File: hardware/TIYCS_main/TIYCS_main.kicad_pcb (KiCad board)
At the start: 2 copper layers, 100 x 100 mm, 46 parts, among them J1 USB4105-GF-A, J2 12vPWM, J3 WS2812B, J4 UART, J5 ExtSensor, J6 Terminal, J7 Barrel_Jack_Switch, J8 pinHeaders, Q1 NCE4060K, Q2 NCE4060K, Q3 2N7002, Q4 NCE4060K, Q5 NCE4060K, SW1 RST, SW2 BOOT, U1 ESP32-WROOM-32U, U2 CH340N, U3 SPX3819M5-L-3-3

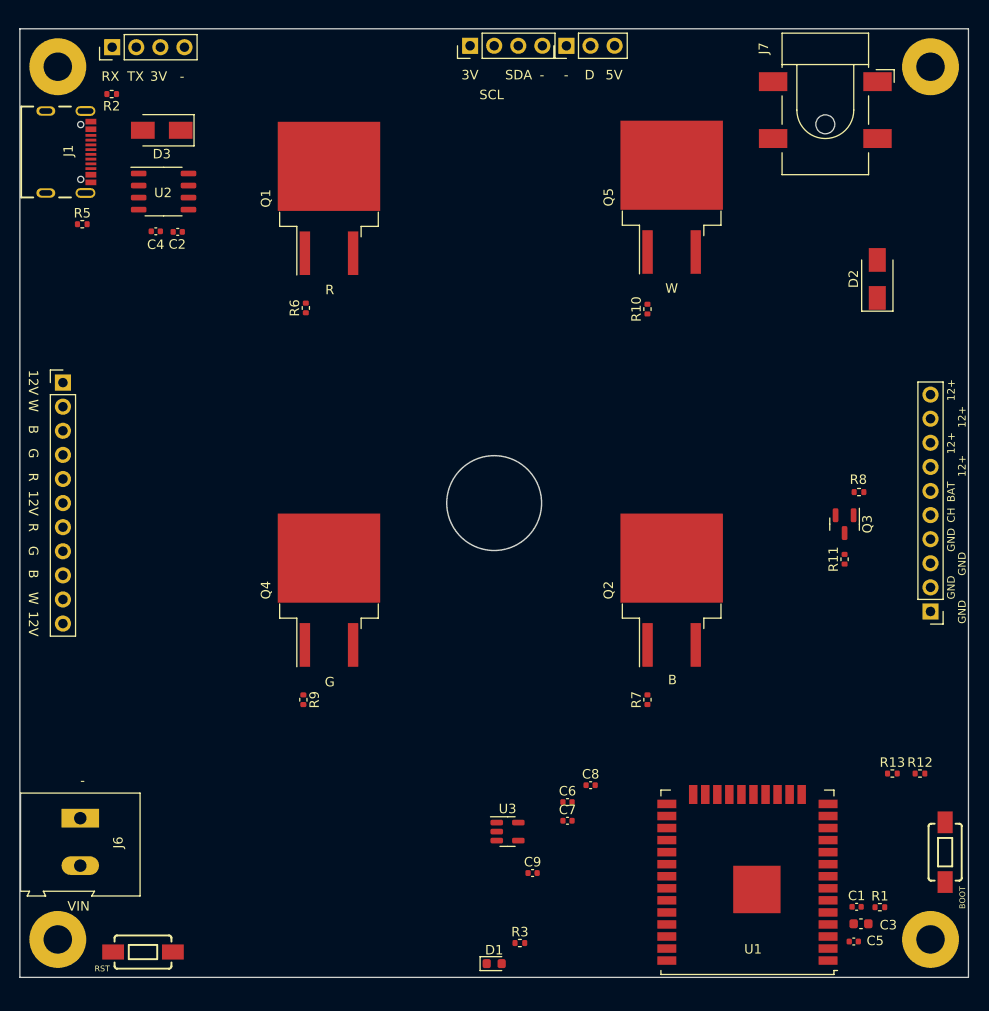
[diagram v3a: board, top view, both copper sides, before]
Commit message: Routed main PCB
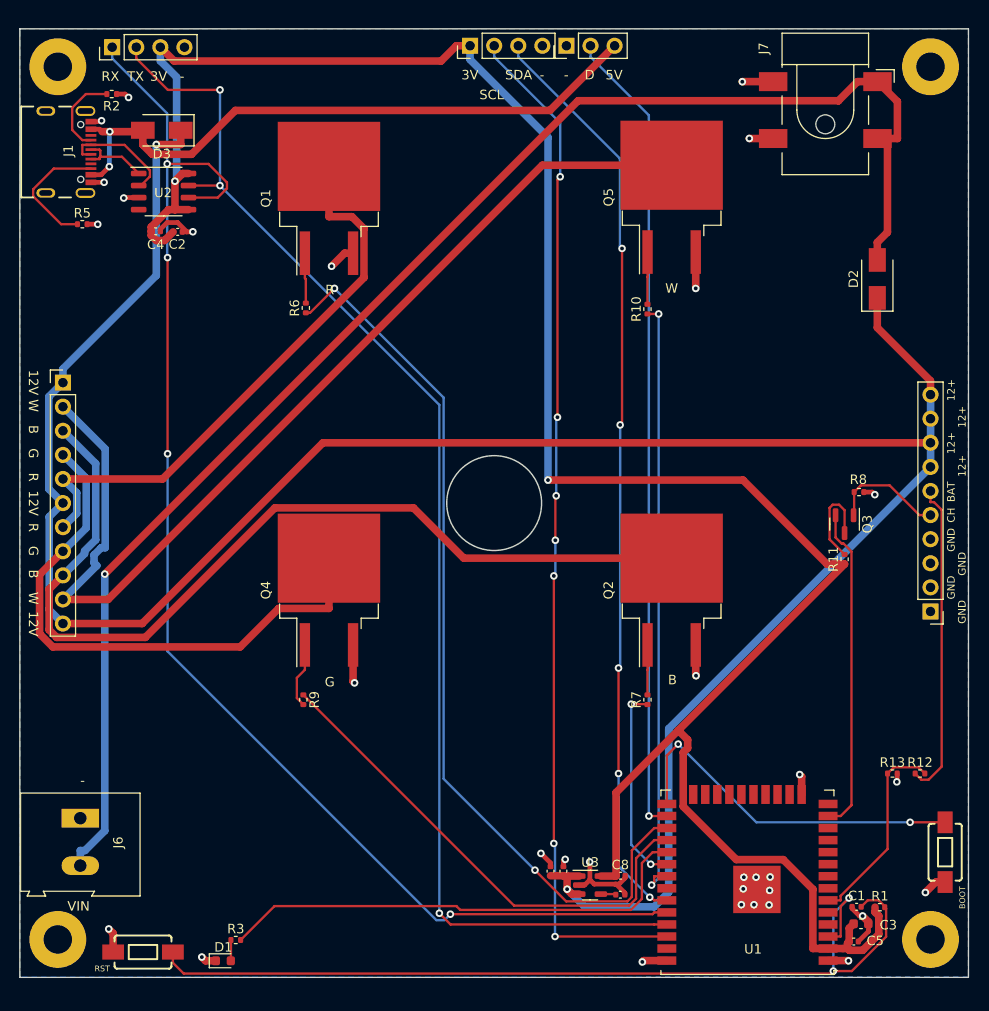
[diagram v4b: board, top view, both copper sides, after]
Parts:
- moved R3 30.0 mm to (22.8, 96.1)
- moved D1 28.6 mm to (21.4, 98.2)
- moved U3 10.4 mm to (60.1, 90.3)
- moved C8 10.0 mm to (63.3, 89.3)
- moved C9 9.53 mm to (63.3, 91.3)
- moved C6 7.29 mm to (57.3, 88.8), turned to -90 degrees
- moved C7 5.60 mm to (55.9, 88.8), turned to -90 degrees
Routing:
- net +12V: track 0.00 -> 254.9 mm, vias 0 -> 2
- net +3V3: track 0.00 -> 236.4 mm, vias 0 -> 2
- net Net-(D2-Pad2): track 0.00 -> 157.3 mm, vias 0 -> 1
- net RX: track 0.00 -> 143.1 mm, vias 0 -> 4
- net TX: track 0.00 -> 135.5 mm, vias 0 -> 3
- net W: track 0.00 -> 112.7 mm
- net SCL: track 0.00 -> 108.9 mm, vias 0 -> 7
- net Net-(C1-Pad2): track 0.00 -> 98.8 mm, vias 0 -> 2
- net B: track 0.00 -> 98.3 mm
- net SDA: track 0.00 -> 98.0 mm, vias 0 -> 5
- net R_PWM: track 0.00 -> 95.5 mm, vias 0 -> 2
- net DATA: track 0.00 -> 85.6 mm, vias 0 -> 1
- net GND: track 0.00 -> 75.6 mm, vias 0 -> 32
- net VUSB: track 0.00 -> 68.0 mm, vias 0 -> 2
- net W_PWM: track 0.00 -> 64.1 mm, vias 0 -> 2
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- added copper zone on B.Cu, net GND

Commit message: Ordered hardware
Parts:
- added 3.3V: TestPoint_Pad_D2.0mm, TestPoint:TestPoint_Pad_D2.0mm, F.Cu at (91.4, 98.1)
- added SW1: NXT, Switches:TACTILE_SWITCH_SMD_6.0X3.5MM, F.Cu at (97.5, 77.0)
- C2, C7, C8: footprint Capacitor_SMD:C_0402_1005Metric -> Capacitor_SMD:C_0603_1608Metric
- moved C8 1.78 mm to (62.6, 87.6)
- moved C2 1.32 mm to (18.0, 21.3)
- moved C7 0.92 mm to (56.0, 87.9)
- moved R12 0.46 mm to (94.4, 78.5)
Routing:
- net unconnected-(U1-Pad23): track 0.00 -> 28.9 mm, vias 0 -> 2
- net GND: track 75.6 -> 80.4 mm
- net +3V3: track 236.4 -> 240.2 mm, vias 2 -> 4
- net V_SENSE_BAT: track 33.4 -> 35.2 mm

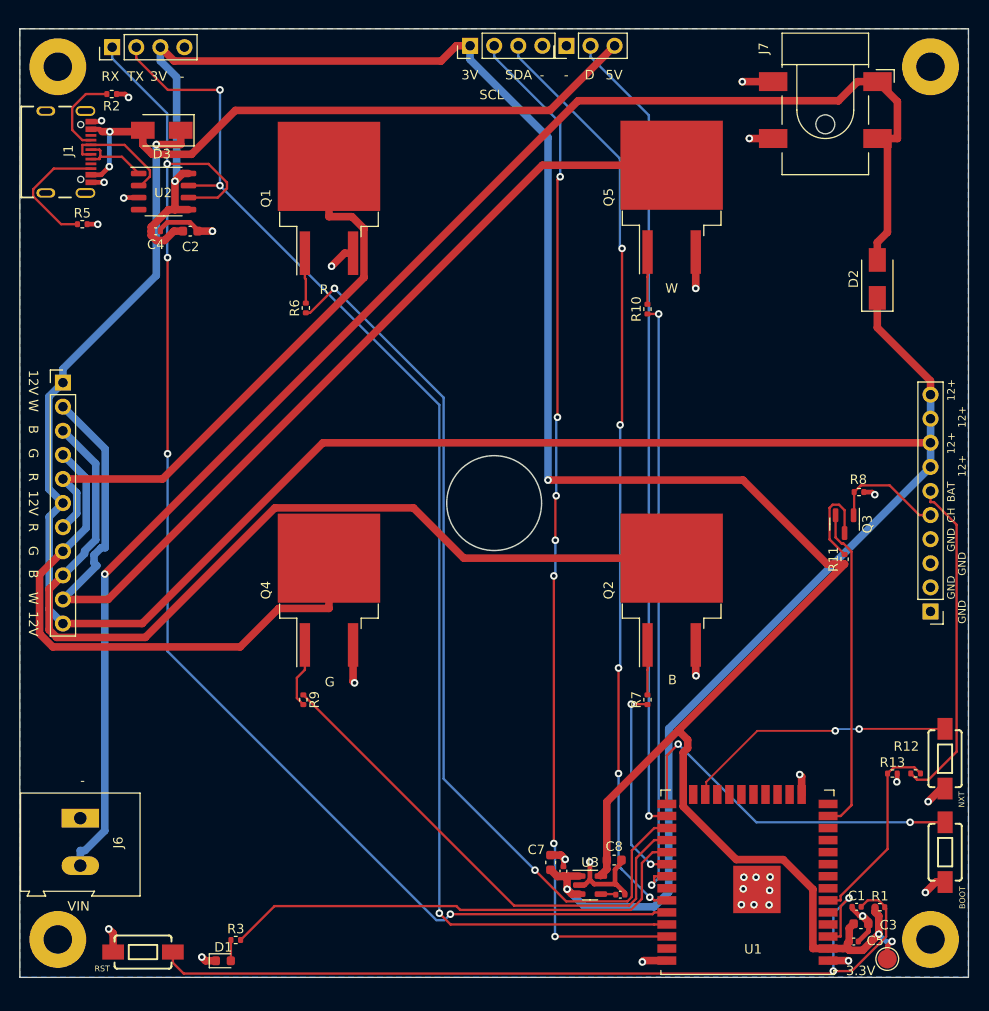
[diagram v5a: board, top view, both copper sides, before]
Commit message: Added XL-1509-3.3 on main board
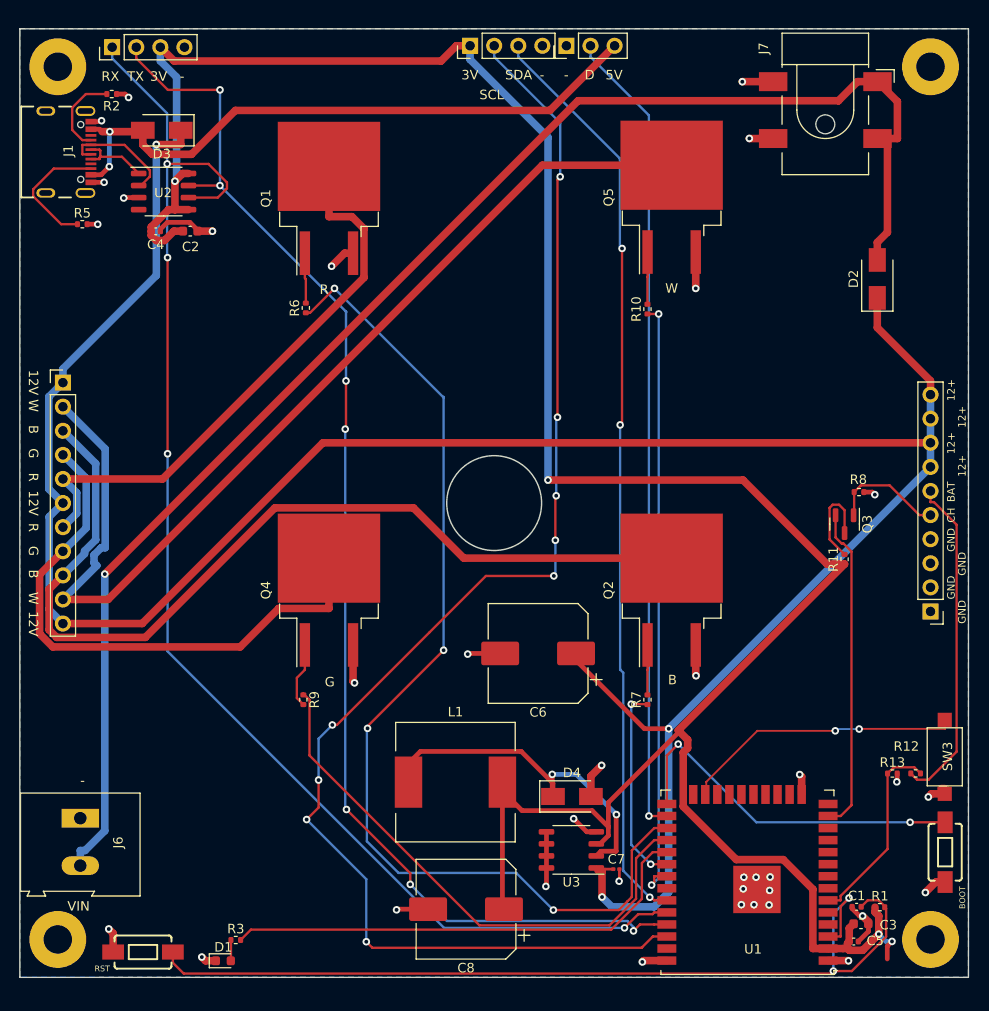
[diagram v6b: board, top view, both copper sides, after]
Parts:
- removed 3.3V: TestPoint_Pad_D2.0mm, TestPoint:TestPoint_Pad_D2.0mm
- removed C9: 10nF, Capacitor_SMD:C_0402_1005Metric
- removed the SW1 at (97.5, 77.0)
- added D4: SS34, Diode_SMD:D_SMA, F.Cu at (58.2, 80.9)
- added L1: 47uH / 2A, Inductor_SMD:L_12x12mm_H8mm, F.Cu at (45.9, 79.4)
- added SW3: BTN, Button_Switch_SMD:SW_SPST_CK_RS282G05A3, F.Cu at (97.5, 76.8)
- C6: value 0.1uF -> 470uF 35V; footprint Capacitor_SMD:C_0402_1005Metric -> Capacitor_SMD:CP_Elec_10x10
- C7: value 10uF -> 1uF; footprint Capacitor_SMD:C_0603_1608Metric -> Capacitor_SMD:C_0201_0603Metric
- C8: value 10uF -> 330uF 35V; footprint Capacitor_SMD:C_0603_1608Metric -> Capacitor_SMD:CP_Elec_10x10
- U3: value SPX3819M5-L-3-3 -> XL-1509-3.3E1; footprint Package_TO_SOT_SMD:SOT-23-5 -> Package_SO:SOP-8_3.9x4.9mm_P1.27mm
- moved C6 23.1 mm to (54.6, 65.8), turned to 180 degrees
- moved C8 16.5 mm to (47.0, 92.8), turned to 180 degrees
- moved C7 6.97 mm to (62.9, 88.6), turned to 0 degrees
- moved U3 4.20 mm to (58.1, 86.6), turned to 180 degrees
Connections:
- C6 pad 1: GND -> +12V
- C6 pad 2: +12V -> GND
- C7 pad 1: GND -> +12V
- C7 pad 2: +12V -> GND
- U1 pad 23: unconnected-(U1-Pad23) -> Net-(SW3-Pad2)
- U3 pad 2: GND -> Net-(D4-Pad1)
- U3 pad 3: +12V -> +3V3
- U3 pad 4: Net-(C9-Pad1) -> GND
- U3 pad 5: +3V3 -> GND
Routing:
- net SCL: track 108.9 -> 147.9 mm, vias 7 -> 9
- net Net-(D4-Pad1): track 0.00 -> 36.0 mm, vias 0 -> 2
- net Net-(SW3-Pad2): track 0.00 -> 29.9 mm, vias 0 -> 2
- net unconnected-(U1-Pad23): track 28.9 -> 0.00 mm, vias 2 -> 0
- net +3V3: track 240.2 -> 263.6 mm
- net R_PWM: track 95.5 -> 111.9 mm, vias 2 -> 4
- net +12V: track 255.4 -> 263.1 mm, vias 2 -> 3
- net GND: track 80.4 -> 88.0 mm, vias 32 -> 36
- net G_PWM: track 52.9 -> 58.4 mm
- net Net-(C9-Pad1): track 1.60 -> 0.00 mm
- net TX: track 135.5 -> 136.5 mm, vias 3 -> 7
- net RX: track 143.1 -> 143.7 mm
- net SDA: track 98.0 -> 97.7 mm, vias 5 -> 3

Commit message: Added XT60 conn to battery board
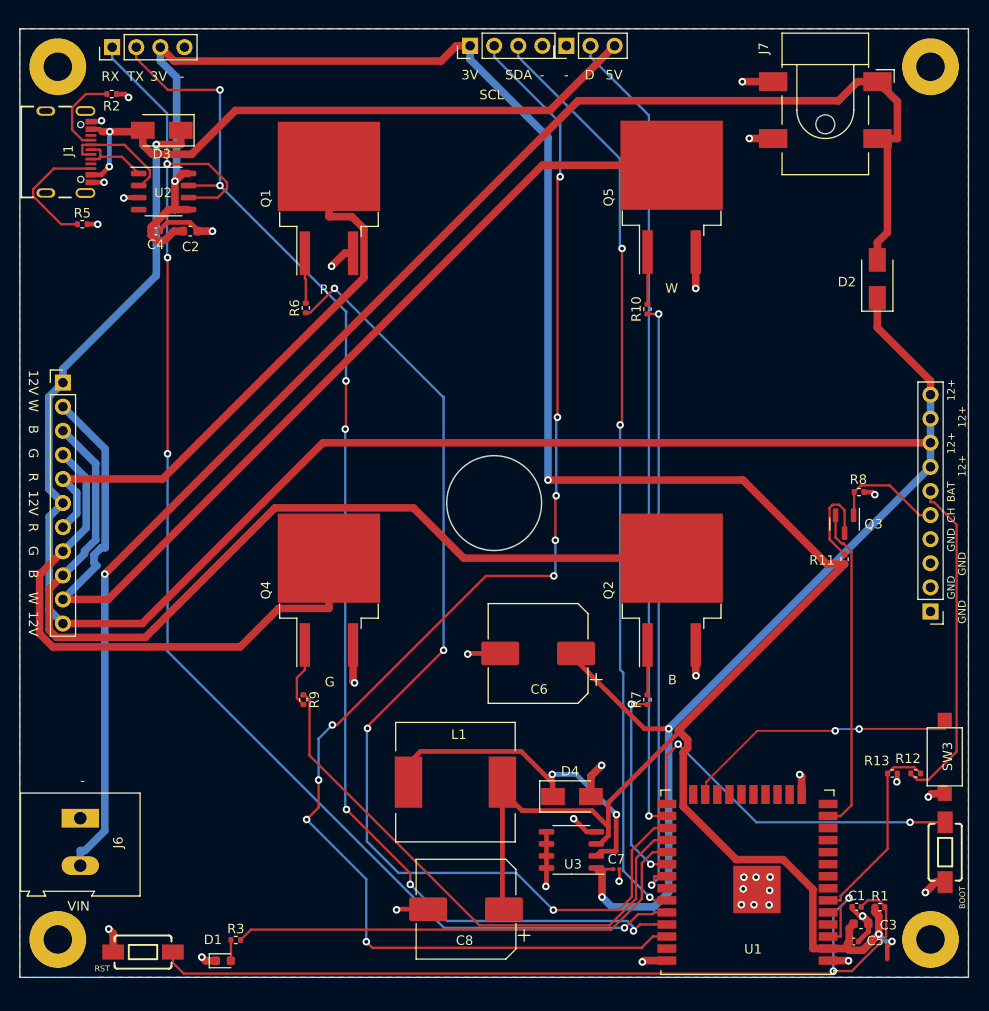
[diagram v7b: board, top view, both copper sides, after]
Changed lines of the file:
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@@
     (property "Sheetname" "")
     (attr smd)
-    (fp_text reference "Q3" (at 0 -2.4 90) (layer "F.SilkS")
+    (fp_text reference "Q3" (at -0.01 -3.05 180) (layer "F.SilkS")
       (effects (font (size 1 1) (thickness 0.15)))
     )
@@
     (property "Sheetname" "")
     (attr smd)
-    (fp_text reference "R13" (at 0 -1.17) (layer "F.SilkS")
+    (fp_text reference "R13" (at -1.65 -1.34) (layer "F.SilkS")
       (effects (font (size 1 1) (thickness 0.15)))
     )
@@
     (property "Sheetname" "")
     (attr smd)
-    (fp_text reference "D2" (at 0 -2.5 90) (layer "F.SilkS")
+    (fp_text reference "D2" (at -0.32 -3.21 180) (layer "F.SilkS")
       (effects (font (size 1 1) (thickness 0.15)))
     )
@@
     (property "Sheetname" "")
     (attr smd)
-    (fp_text reference "C6" (at 0 -6.2) (layer "F.SilkS")
+    (fp_text reference "C6" (at -0.11 -3.79) (layer "F.SilkS")
       (effects (font (size 1 1) (thickness 0.15)))
     )
@@
     (property "Sheetname" "")
     (attr smd)
-    (fp_text reference "U3" (at 0 -3.4) (layer "F.SilkS")
+    (fp_text reference "U3" (at -0.17 -1.51) (layer "F.SilkS")
       (effects (font (size 1 1) (thickness 0.15)))
     )
@@
     (property "Sheetname" "")
     (attr smd)
-    (fp_text reference "D4" (at 0 -2.5) (layer "F.SilkS")
+    (fp_text reference "D4" (at -0.2 -2.66) (layer "F.SilkS")
       (effects (font (size 1 1) (thickness 0.15)))
     )
@@
     (property "Sheetname" "")
     (attr smd)
-    (fp_text reference "C8" (at 0 -6.2) (layer "F.SilkS")
+    (fp_text reference "C8" (at 0.1525 -3.3) (layer "F.SilkS")
       (effects (font (size 1 1) (thickness 0.15)))
     )
@@
     (property "Sheetname" "")
     (attr smd)
-    (fp_text reference "L1" (at 0 -7.4) (layer "F.SilkS")
+    (fp_text reference "L1" (at 0.35 -5.02) (layer "F.SilkS")
       (effects (font (size 1 1) (thickness 0.15)))
     )
@@
     (property "Sheetname" "")
     (attr smd)
-    (fp_text reference "D1" (at 0 -1.43) (layer "F.SilkS")
+    (fp_text reference "D1" (at -1.1 -2.22) (layer "F.SilkS")
       (effects (font (size 1 1) (thickness 0.15)))
     )
@@
     (property "Sheetname" "")
     (attr smd)
-    (fp_text reference "R11" (at 0 -1.17 90) (layer "F.SilkS")
+    (fp_text reference "R11" (at -0.11 -2.38 180) (layer "F.SilkS")
       (effects (font (size 1 1) (thickness 0.15)))
     )
@@
     (property "Sheetname" "")
     (attr smd)
-    (fp_text reference "R12" (at -0.98 -2.85) (layer "F.SilkS")
-      (effects (font (size 1 1) (thickness 0.15)))
-    )
+    (fp_text reference "R12" (at -0.81 -1.56) (layer "F.SilkS")
+      (effects (font (size 1 1) (thickness 0.15)))
+    )

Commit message: Updated README
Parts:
- added R4: 10K, Resistor_SMD:R_0603_1608Metric, F.Cu at (88.3, 46.2)
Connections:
- Q3 pad 1: V_SENSE -> Net-(Q3-Pad1)
- R8 pad 2: V_SENSE -> Net-(Q3-Pad1)
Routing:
- net Net-(Q3-Pad1): track 0.00 -> 4.31 mm
- net V_SENSE: track 12.1 -> 10.1 mm
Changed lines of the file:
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@@
   (net 58 "unconnected-(U2-Pad4)")
   (net 59 "ADC")
+  (net 60 "Net-(Q3-Pad1)")
   (footprint "Resistor_SMD:R_0402_1005Metric" (layer "F.Cu")
     (at 66.16 70.73 90)
@@
     (fp_line (start -0.325 -1.45) (end 0.65 -1.45) (layer "F.Fab") (width 0.1))
     (pad "1" smd roundrect locked (at -0.9375 -0.95 270) (size 1.475 0.6) (layers "F.Cu" "F.Paste" "F.Mask") (roundrect_rratio 0.25)
-      (net 24 "V_SENSE") (pinfunction "G") (pintype "input"))
+      (net 60 "Net-(Q3-Pad1)") (pinfunction "G") (pintype "input"))
     (pad "2" smd roundrect locked (at -0.9375 0.95 270) (size 1.475 0.6) (layers "F.Cu" "F.Paste" "F.Mask") (roundrect_rratio 0.25)
       (net 28 "SENSE_PIN") (pinfunction "S") (pintype "passive"))
@@
       (net 1 "GND") (pintype "passive"))
     (model "${KICAD6_3DMODEL_DIR}/Capacitor_SMD.3dshapes/C_0603_1608Metric.wrl"
+      (offset (xyz 0 0 0))
+      (scale (xyz 1 1 1))
+      (rotate (xyz 0 0 0))
+    )
+  )
+  (footprint "Resistor_SMD:R_0603_1608Metric" (layer "F.Cu")
+    (at 88.3 46.23 -90)
+    (descr "Resistor SMD 0603 (1608 Metric), square (rectangular) end terminal, IPC_7351 nominal, (Body size source: IPC-SM-782 page 72, https://www.pcb-3d.com/wordpress/wp-content/uploads/ipc-sm-782a_amendment_1_and_2.pdf), generated with kicad-footprint-generator")
+    (tags "resistor")
+    (property "Sheetfile" "TIYCS_main.kicad_sch")
+    (property "Sheetname" "")
+    (attr smd)
+    (fp_text reference "R4" (at 0.22 -2.03 180) (layer "F.SilkS")
+      (effects (font (size 1 1) (thickness 0.15)))
+    )
+    (fp_text value "10K" (at 0 1.43 90) (layer "F.Fab")
+      (effects (font (size 1 1) (thickness 0.15)))
+    )
+    (fp_text user "${REFERENCE}" (at 0 0 90) (layer "F.Fab")
+      (effects (font (size 0.4 0.4) (thickness 0.06)))
+    )
+    (fp_line (start -0.237258 -0.5225) (end 0.237258 -0.5225) (layer "F.SilkS") (width 0.12))
+    (fp_line (start -0.237258 0.5225) (end 0.237258 0.5225) (layer "F.SilkS") (width 0.12))
+    (fp_line (start 1.48 0.73) (end -1.48 0.73) (layer "F.CrtYd") (width 0.05))
+    (fp_line (start -1.48 0.73) (end -1.48 -0.73) (layer "F.CrtYd") (width 0.05))
+    (fp_line (start 1.48 -0.73) (end 1.48 0.73) (layer "F.CrtYd") (width 0.05))
+    (fp_line (start -1.48 -0.73) (end 1.48 -0.73) (layer "F.CrtYd") (width 0.05))
+    (fp_line (start -0.8 0.4125) (end -0.8 -0.4125) (layer "F.Fab") (width 0.1))
+    (fp_line (start 0.8 -0.4125) (end 0.8 0.4125) (layer "F.Fab") (width 0.1))
+    (fp_line (start 0.8 0.4125) (end -0.8 0.4125) (layer "F.Fab") (width 0.1))
+    (fp_line (start -0.8 -0.4125) (end 0.8 -0.4125) (layer "F.Fab") (width 0.1))
+    (pad "1" smd roundrect locked (at -0.825 0 270) (size 0.8 0.95) (layers "F.Cu" "F.Paste" "F.Mask") (roundrect_rratio 0.25)
+      (net 24 "V_SENSE") (pintype "passive"))
+    (pad "2" smd roundrect locked (at 0.825 0 270) (size 0.8 0.95) (layers "F.Cu" "F.Paste" "F.Mask") (roundrect_rratio 0.25)
+      (net 60 "Net-(Q3-Pad1)") (pintype "passive"))
+    (model "${KICAD6_3DMODEL_DIR}/Resistor_SMD.3dshapes/R_0603_1608Metric.wrl"
       (offset (xyz 0 0 0))
       (scale (xyz 1 1 1))
@@
     (property "Sheetname" "")
     (attr smd)
-    (fp_text reference "R8" (at 0.07 1.32) (layer "F.SilkS")
+    (fp_text reference "R8" (at 2.26 0) (layer "F.SilkS")
       (effects (font (size 1 1) (thickness 0.15)))
     )
@@
       (net 1 "GND") (pintype "passive"))
     (pad "2" smd roundrect locked (at 0.51 0 180) (size 0.54 0.64) (layers "F.Cu" "F.Paste" "F.Mask") (roundrect_rratio 0.25)
-      (net 24 "V_SENSE") (pintype "passive"))
+      (net 60 "Net-(Q3-Pad1)") (pintype "passive"))
     (model "${KICAD6_3DMODEL_DIR}/Resistor_SMD.3dshapes/R_0402_1005Metric.wrl"
       (offset (xyz 0 0 0))
@@
   (segment (start 62.88902 82.84) (end 58.64902 78.6) (width 0.5) (layer "B.Cu") (net 23))
   (segment (start 96 51.265) (end 94.8247 51.265) (width 0.25) (layer "F.Cu") (net 24))
-  (segment (start 94.8247 51.265) (end 91.6917 48.132) (width 0.25) (layer "F.Cu") (net 24))
-  (segment (start 87.95 51.2225) (end 87.89 51.2825) (width 0.25) (layer "F.Cu") (net 24))
-  (segment (start 91.6917 48.132) (end 88.658 48.132) (width 0.25) (layer "F.Cu") (net 24))
-  (segment (start 88.658 48.132) (end 87.95 48.84) (width 0.25) (layer "F.Cu") (net 24))
-  (segment (start 87.95 48.84) (end 87.95 51.2225) (width 0.25) (layer "F.Cu") (net 24))
+  (segment (start 88.3 45.405) (end 88.9647 45.405) (width 0.25) (layer "F.Cu") (net 24))
+  (segment (start 88.9647 45.405) (end 94.8247 51.265) (width 0.25) (layer "F.Cu") (net 24))
   (segment (start 12.8936 62.7) (end 31.9486 43.645) (width 0.8) (layer "F.Cu") (net 25))
   (segment (start 16.96 10.7) (end 16.96 12.2003) (width 0.8) (layer "F.Cu") (net 25))
@@
   (segment (start 94.2944 77.8544) (end 92.1256 77.8544) (width 0.25) (layer "F.Cu") (net 59))
   (segment (start 94.94 78.5) (end 94.2944 77.8544) (width 0.25) (layer "F.Cu") (net 59))
+  (segment (start 88.3 47.055) (end 88.3 48.43) (width 0.25) (layer "F.Cu") (net 60))
+  (segment (start 87.95 51.2225) (end 87.89 51.2825) (width 0.25) (layer "F.Cu") (net 60))
+  (segment (start 88.3 48.43) (end 87.97 48.76) (width 0.25) (layer "F.Cu") (net 60))
+  (segment (start 87.95 48.84) (end 87.95 51.2225) (width 0.25) (layer "F.Cu") (net 60))
   (zone (net 1) (net_name "GND") (layer "B.Cu") (hatch edge 0.508)
     (connect_pads (clearance 0.508))
